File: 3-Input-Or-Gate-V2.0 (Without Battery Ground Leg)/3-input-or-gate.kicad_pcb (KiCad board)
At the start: 2 copper layers, 9.4 x 11 mm, 12 parts, among them U5 74LVC1G332GW,125

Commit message: Updated files to
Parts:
- C1: value 0.01uf -> 0.01uf (maybe 100uf)
- moved ? 0.67 mm to (146.9, 99.6)
- moved C1 0.51 mm to (147.3, 93.9)
- moved U5 0.48 mm to (149.6, 96.6)
- moved ? 0.46 mm to (145.8, 98.6)
- moved R2 0.18 mm to (146.8, 97.0)
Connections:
- ? pad 1: VCC-PAD -> VCC5V
- C1 pad 5: VCC-PAD -> VCC5V
- R1 pad 2: VCC-PAD -> VCC5V
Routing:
- net VCC5V: track 4.57 -> 19.4 mm, vias 0 -> 2
- net VCC-PAD: track 9.82 -> 0.00 mm
- net CE: track 9.24 -> 10.3 mm
- net C: track 7.20 -> 6.48 mm
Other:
- board text added: "VCC 5V"
- board text removed: "VCC"

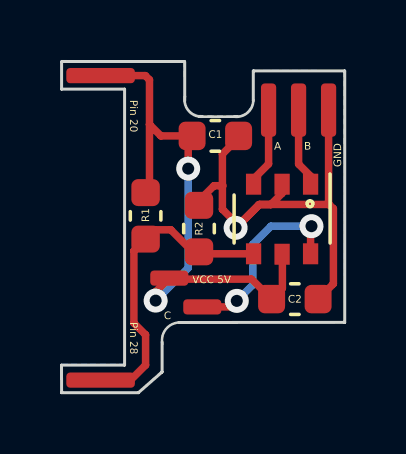
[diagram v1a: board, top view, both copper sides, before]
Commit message: Changed footprint of or gate to be more in line with the IC
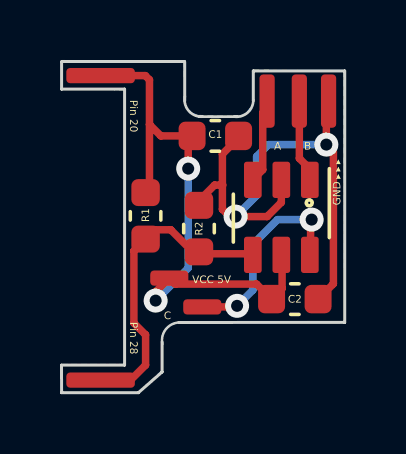
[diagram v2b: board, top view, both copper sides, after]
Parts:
- moved ? 0.30 mm to (149.1, 92.7)
- moved ? 0.30 mm to (150.1, 92.7)
- moved ? 0.30 mm to (151.1, 92.7)
- moved U5 0.18 mm to (149.5, 96.5)
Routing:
- net GND: track 16.5 -> 18.8 mm, vias 1 -> 2
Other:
- board text added: "▲ ▲ ▲"
